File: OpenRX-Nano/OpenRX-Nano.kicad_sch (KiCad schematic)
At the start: 0 parts

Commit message: Fix passive footprints to 0402/0603, add LCSC part numbers
- All caps/resistors: 0201 → 0402 (1005 Metric)
- 10uF bulk caps: 0402 → 0603 (1608 Metric)
- Added LCSC field to all 23 passives:
  100nF=C1525, 1uF=C52923, 10uF=C15525, 10pF=C32949,
  470nF=C1543, 1nF=C1523, 10k=C25744
- All JLCPCB basic parts, zero extended part setup fees on passives
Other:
- added sheet ESP32-C3 + SX1281 Core (../shared/sheets/esp32c3_sx1281_rx_core.kicad_sch)
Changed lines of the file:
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@@
 (kicad_sch
-  (version 20231120)
-  (generator "eeschema")
-  (generator_version "9.0")
-  (paper "A3")
-  (symbol_instances)
+	(version 20260306)
+	(generator "eeschema")
+	(generator_version "10.0")
+	(paper "A3")
+	(sheet
+		(at 25.4 25.4)
+		(size 66.04 113.03)
+		(exclude_from_sim no)
+		(in_bom yes)
+		(on_board yes)
+		(dnp no)
+		(stroke
+			(width 0.1524)
+			(type solid)
+		)
+		(fill
+			(color 0 0 0 0)
+		)
+		(property "Sheetname" "ESP32-C3 + SX1281 Core"
+			(at 25.4 24.6888 0)
+			(show_name no)
+			(do_not_autoplace no)
+			(effects
+				(font
+					(size 1.27 1.27)
+				)
+				(justify left bottom)
+			)
+		)
+		(property "Sheetfile" "../shared/sheets/esp32c3_sx1281_rx_core.kicad_sch"
+			(at 25.4 141.478 0)
+			(show_name no)
+			(do_not_autoplace no)
+			(effects
+				(font
+					(size 1.27 1.27)
+				)
+				(justify left top)
+			)
+		)
+	)
+	(sheet_instances
+		(path "/"
+			(page "1")
+		)
+	)
+	(embedded_fonts no)
 )

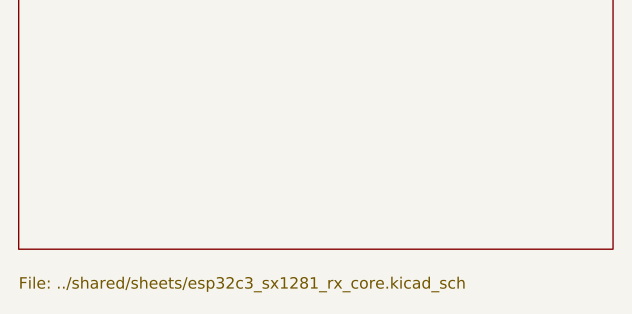
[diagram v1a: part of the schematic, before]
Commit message: Separate Lite and Nano schematics, stop sharing one file
Sharing one .kicad_sch between projects doesn't work - KiCad
overwrites instance data when either project saves.

- Lite: restored pre-Nano schematic as local esp32c3_sx1281_lite.kicad_sch
- Nano: copied current shared sheet as local esp32c3_sx1281_rx_core.kicad_sch
- Each project now has its own schematic file
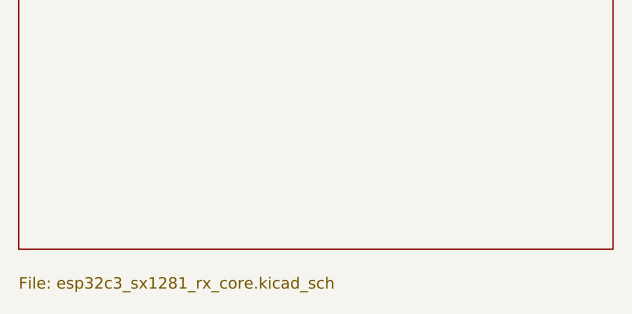
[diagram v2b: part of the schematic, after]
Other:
- sheet ESP32-C3 + SX1281 Core: file ../shared/sheets/esp32c3_sx1281_rx_core.kicad_sch -> esp32c3_sx1281_rx_core.kicad_sch
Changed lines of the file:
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@@
 			)
 		)
-		(property "Sheetfile" "../shared/sheets/esp32c3_sx1281_rx_core.kicad_sch"
+		(property "Sheetfile" "esp32c3_sx1281_rx_core.kicad_sch"
 			(at 25.4 141.478 0)
 			(show_name no)
